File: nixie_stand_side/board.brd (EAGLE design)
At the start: 25 x 30 mm, 2 parts

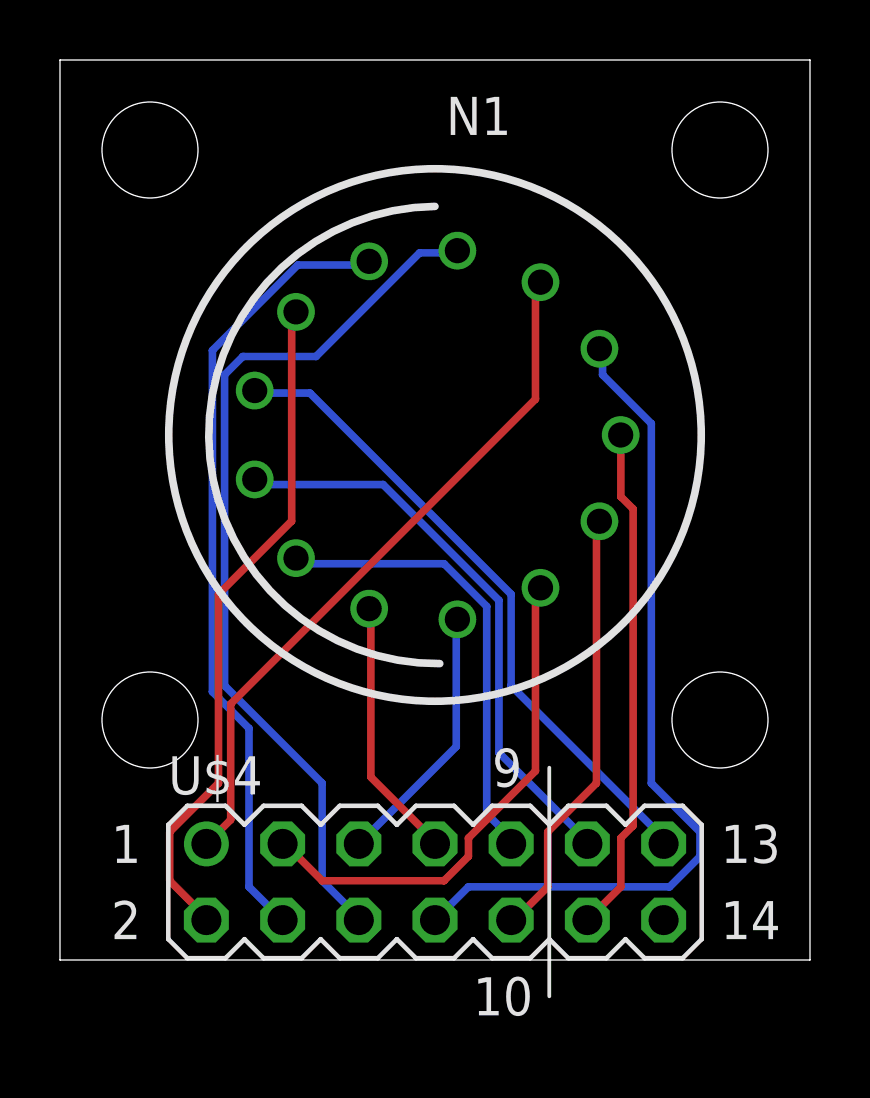
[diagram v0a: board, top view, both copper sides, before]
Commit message: [fix] 太さ・ガーバー出力(FusionPCB)
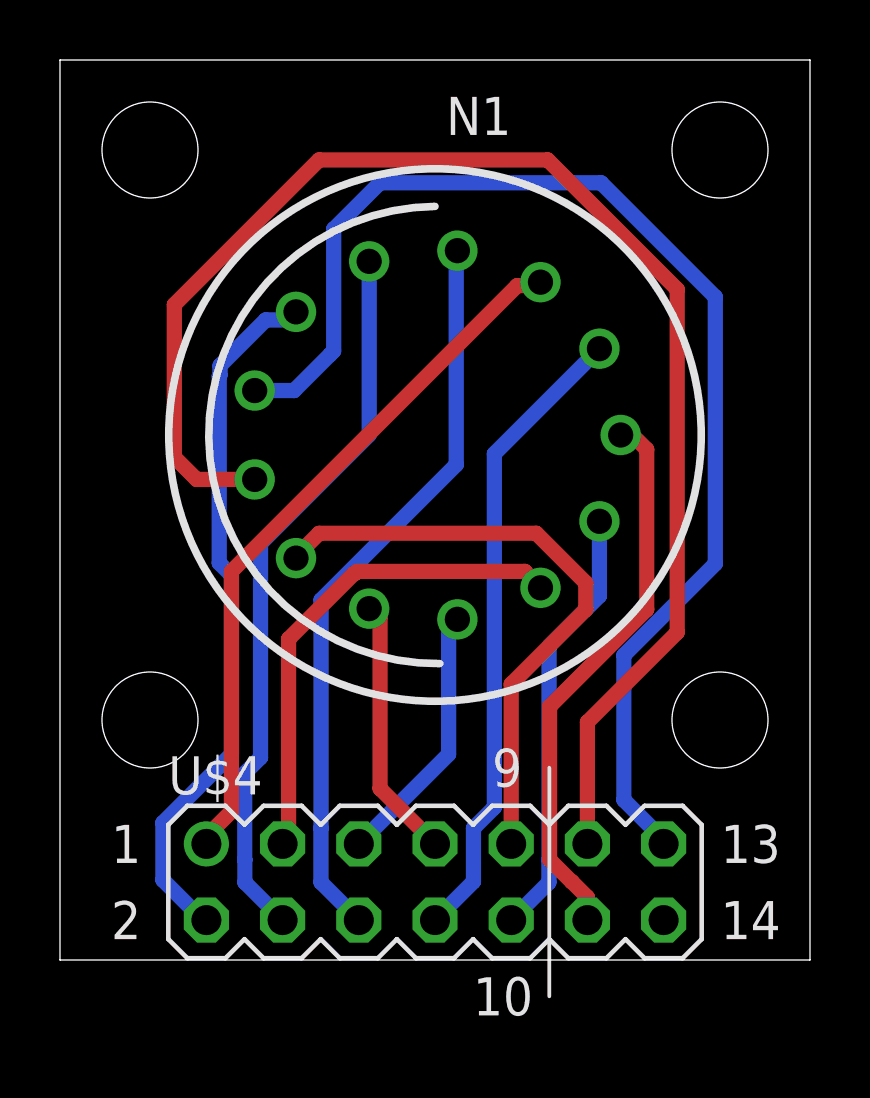
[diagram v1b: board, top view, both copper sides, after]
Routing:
- net NIXIE5: track 19.2 -> 48.3 mm
- net NIXIE6: track 21.8 -> 42.2 mm
- net N$2: track 28.0 -> 21.3 mm
- net NIXIE4: track 15.3 -> 20.5 mm
- net NIXIE9: track 29.5 -> 24.7 mm
- net NIXIE8: track 26.4 -> 24.2 mm
- net N$1: track 17.0 -> 18.6 mm
- net NIXIE7: track 22.6 -> 23.5 mm
- net NIXIE1: track 17.1 -> 16.5 mm
